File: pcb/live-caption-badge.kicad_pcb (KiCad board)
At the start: 4 copper layers, 170 x 100 mm, 102 parts, among them J1 Conn_01x09, J2 Conn_01x06, J3 Conn_01x09, J4 AudioJack4, J5 USB_C_Receptacle_USB2.0_16P, SW1 SW_DPDT_x2, SW2 RST, SW3 BTN, SW4 BTN, SW5 BTN, SW6 RST, U1 ESP32-S3-WROOM-1, U2 HE9073A33M5R, U3 HE9073A33M5R, U4 ES7210, U5 ES8311, U6 IS31AP2005

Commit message: pcb: Yippee
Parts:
- added R15: 1M, Resistor_SMD:R_0603_1608Metric, F.Cu at (74.0, 75.0)
- added R16: 2M, Resistor_SMD:R_0603_1608Metric, F.Cu at (74.0, 72.0)
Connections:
- U1 pad 15: unconnected-(U1-IO3-Pad15) -> /BATT_ADC
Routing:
- net /BATT_ADC: track 0.00 -> 26.7 mm
- net +BATT: track 50.2 -> 71.6 mm
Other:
- board text added: "M3"
- board text added: "yeah it wasn't soldered very well"

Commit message: pcb: Slap a KiCad logo on it
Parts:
- added REF**: KiCad-Logo2_8mm_Copper, Symbol:KiCad-Logo2_8mm_Copper, F.Cu at (180.0, 116.0)

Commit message: pcb: Edit a couple R/C values, generate BOM
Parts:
- R15: value 1M -> 150k
- R16: value 2M -> 300k
- R6: value 1k -> 5.1k
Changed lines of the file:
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@@
 			)
 		)
-		(property "Value" "1k"
+		(property "Value" "5.1k"
 			(at 0 1.43 0)
 			(layer "F.Fab")
@@
 		)
 		(fp_text user "${REFERENCE}"
-			(at 0 6.35 360)
+			(at 0 6.35 0)
 			(layer "F.Fab")
 			(effects
@@
 			)
 		)
-		(property "Value" "2M"
+		(property "Value" "300k"
 			(at 0 1.43 0)
 			(layer "F.Fab")
@@
 		(tags "resistor")
 		(property "Reference" "R15"
-			(at 0 1.5 360)
+			(at 0 1.5 0)
 			(layer "F.SilkS")
 			(effects
@@
 			)
 		)
-		(property "Value" "1M"
-			(at 0 1.43 360)
+		(property "Value" "150k"
+			(at 0 1.43 0)
 			(layer "F.Fab")
 			(effects
@@
 		)
 		(fp_text user "${REFERENCE}"
-			(at 0 0 360)
+			(at 0 0 0)
 			(layer "F.Fab")
 			(effects

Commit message: pcb: Rev 2 schematic
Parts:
- removed J1: Conn_01x09, live-caption-badge:Molex_CLIK-Mate_502386-0970_1x09-1MP_P1.25mm_Horizontal
- removed J3: Conn_01x09, Connector_PinHeader_2.54mm:PinHeader_1x09_P2.54mm_Vertical
- removed the REF** at (144.0, 102.5)
- removed the REF** at (144.0, 116.5)
- removed the REF** at (86.0, 102.5)
- removed the REF** at (144.0, 125.4)
- removed the REF** at (86.0, 125.4)
- removed the REF** at (86.0, 116.5)
- added C36: 1uF, Capacitor_SMD:C_0603_1608Metric, F.Cu at (225.2, 89.8)
- added C37: 10uF, Capacitor_SMD:C_0603_1608Metric, F.Cu at (225.2, 92.4)
- added C38: 1uF, Capacitor_SMD:C_0603_1608Metric, F.Cu at (225.2, 94.9)
- added C39: 1uF, Capacitor_SMD:C_0603_1608Metric, F.Cu at (225.2, 97.4)
- added C40: 1uF, Capacitor_SMD:C_0603_1608Metric, F.Cu at (225.2, 99.9)
- added C41: 10uF, Capacitor_SMD:C_0603_1608Metric, F.Cu at (229.2, 89.8)
- added C42: 10uF, Capacitor_SMD:C_0603_1608Metric, F.Cu at (229.2, 92.4)
- added C43: 10uF, Capacitor_SMD:C_0603_1608Metric, F.Cu at (229.2, 94.9)
- added C44: 10uF, Capacitor_SMD:C_0603_1608Metric, F.Cu at (229.2, 97.4)
- added C45: 1uF, Capacitor_SMD:C_0603_1608Metric, F.Cu at (229.2, 99.9)
- added C46: 10uF, Capacitor_SMD:C_0603_1608Metric, F.Cu at (233.2, 89.8)
- added C47: 4.7uF, Capacitor_SMD:C_0603_1608Metric, F.Cu at (235.0, 113.0)
- added C6: 47uF, Capacitor_SMD:C_0603_1608Metric, F.Cu at (239.2, 96.5)
- added D2: MBR0530, Diode_SMD:D_SOD-123, F.Cu at (244.0, 110.0)
- added D3: MBR0530, Diode_SMD:D_SOD-123, F.Cu at (244.0, 115.0)
- added D4: MBR0530, Diode_SMD:D_SOD-123, F.Cu at (244.0, 120.0)
- added Q1: Si1308EDL, Package_TO_SOT_SMD:SOT-323_SC-70, F.Cu at (235.0, 120.0)
- added R17: 0.47, Resistor_SMD:R_0603_1608Metric, F.Cu at (227.0, 121.0)
- added R7: 10k, Resistor_SMD:R_0603_1608Metric, F.Cu at (227.0, 118.0)
- added TP17: TestPoint, Connector_PinHeader_2.54mm:PinHeader_1x01_P2.54mm_Vertical, F.Cu at (133.0, 73.0)
- C1: footprint Capacitor_SMD:C_0603_1608Metric -> Capacitor_THT:CP_Radial_D8.0mm_P3.50mm
- moved C1 77.5 mm to (70.5, 111.0)
- moved J5 1.23 mm to (52.0, 32.1)
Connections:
- U1 pad 8: /SPI_CS -> /SPI_~{CS}
- U6 pad 5: /Audio/AUDIO_OUT -> Net-(C6-Pad1)
- U6 pad 8: GNDA -> unconnected-(U6-Pad8)
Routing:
- net /SPI_CS: track 70.7 -> 0.00 mm, vias 2 -> 0
- net /USB_D+: track 24.4 -> 0.00 mm
- net /USB_D-: track 24.2 -> 0.00 mm
- net Net-(J5-CC2): track 16.8 -> 0.00 mm
- net Net-(J5-CC1): track 14.5 -> 0.00 mm
- net GND: track 16.8 -> 4.86 mm
- net /Audio/AUDIO_OUT: track 56.3 -> 47.3 mm
- net +3V3: track 39.6 -> 32.4 mm
- net /EPD_PWR: track 83.3 -> 76.0 mm
- net /EPD_~{BUSY}: track 51.3 -> 44.6 mm
- net /SPI_MOSI: track 42.6 -> 36.4 mm
- net /SPI_SCK: track 44.0 -> 38.3 mm
- net /EPD_DC: track 60.9 -> 55.2 mm
- net GNDA: track 17.6 -> 19.3 mm
- net VBUS: track 54.1 -> 53.3 mm
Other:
- outline, holes or cut-outs redrawn
- board text removed: "BUSY"
- board text removed: "CS"
- board text removed: "DC"
- board text removed: "MOSI"
- board text removed: "PWR"
- board text removed: "RST"
- board text removed: "SCK"

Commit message: pcb: rev 2?
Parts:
- added J1: Conn_01x24, live-caption-badge:FPC05024-13200_1x24-1MP_P0.50_Horizontal, F.Cu at (115.0, 117.0)
- added L1: 68uH, live-caption-badge:L_Bourns-SDEE0406A, F.Cu at (123.5, 100.0)
- added Q2: SS8050, Package_TO_SOT_SMD:SOT-23, F.Cu at (110.0, 47.0)
- added Q3: SS8050, Package_TO_SOT_SMD:SOT-23, F.Cu at (110.0, 53.0)
- added R18: 10k, Resistor_SMD:R_0603_1608Metric, F.Cu at (115.0, 48.0)
- added R19: 10k, Resistor_SMD:R_0603_1608Metric, F.Cu at (115.0, 54.0)
- SW6: value RST -> FLASH
- moved C46 127.7 mm to (106.0, 101.0), turned to 180 degrees
- moved D4 124.5 mm to (120.0, 109.0), turned to 90 degrees
- moved C36 120.9 mm to (106.0, 110.0), turned to 180 degrees
- moved D3 120.1 mm to (124.0, 109.0), turned to -90 degrees
- moved C37 120.1 mm to (106.0, 107.0), turned to 180 degrees
- moved C38 119.5 mm to (106.0, 104.0), turned to 180 degrees
- moved D2 116.0 mm to (128.0, 109.0), turned to 90 degrees
- moved Q1 104.1 mm to (133.0, 99.0), turned to 90 degrees
- moved C47 102.0 mm to (133.0, 110.0), turned to 0 degrees
- moved C42 102.0 mm to (130.5, 118.0)
- moved C44 100.3 mm to (130.5, 115.0)
- moved C41 98.7 mm to (135.5, 121.0)
- moved C39 98.4 mm to (130.5, 124.0)
- moved C40 97.0 mm to (130.5, 121.0)
- moved C43 96.5 mm to (135.5, 118.0)
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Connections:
- C4 pad 1: /ESP_EN -> /ESP_~{EN}
- J2 pad 4: /ESP_IO0 -> /UART_RTS
- J2 pad 5: /ESP_EN -> /UART_DTR
- R1 pad 2: /ESP_EN -> /ESP_~{EN}
- SW2 pad 2: /ESP_EN -> /ESP_~{EN}
- U1 pad 19: /EPD_DC -> /EPD_~{BUSY}
- U1 pad 21: /SPI_SCK -> /EPD_DC
- U1 pad 22: /SPI_MOSI -> /SPI_~{CS}
- U1 pad 23: unconnected-(U1-IO21-Pad23) -> /SPI_SCK
- U1 pad 24: /EPD_~{BUSY} -> /SPI_MOSI
- U1 pad 3: /ESP_EN -> /ESP_~{EN}
- U1 pad 7: /EPD_PWR -> unconnected-(U1-IO7-Pad7)
- U1 pad 8: /SPI_~{CS} -> unconnected-(U1-IO15-Pad8)
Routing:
- net /ESP_~{EN}: track 0.00 -> 87.4 mm, vias 0 -> 2
- net /ESP_EN: track 79.2 -> 0.00 mm, vias 3 -> 0
- net /SPI_~{CS}: track 0.00 -> 76.8 mm
- net /EPD_PWR: track 76.0 -> 0.00 mm, vias 2 -> 0
- net /ESP_IO0: track 80.6 -> 38.7 mm, vias 3 -> 0
- net /SPI_MOSI: track 36.4 -> 77.2 mm, vias 1 -> 0
- net /SPI_SCK: track 38.3 -> 76.4 mm
- net /E-Paper/GDR: track 0.00 -> 36.3 mm, vias 0 -> 2
- net /E-Paper/RESE: track 0.00 -> 33.2 mm, vias 0 -> 2
- net /EPD_~{BUSY}: track 44.6 -> 77.7 mm, vias 1 -> 0
- net Net-(D4-A): track 0.00 -> 32.8 mm
- net /USB_D+: track 0.00 -> 26.4 mm
- net /USB_D-: track 0.00 -> 25.0 mm, vias 0 -> 2
- net /UART_RTS: track 0.00 -> 22.6 mm, vias 0 -> 1
- net /EPD_DC: track 55.2 -> 77.1 mm, vias 2 -> 0
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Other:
- outline, holes or cut-outs redrawn
- board text added: ":3"
- board text added: "BTN1"
- board text added: "BTN2"
- board text added: "BTN3"
- board text added: "DTR"
- board text added: "LIVE CAPTION BADGE REV 2 EECS 473 FA 2024"
- board text added: "RTS"
- board text added: "do not detonate"
- board text removed: "EN"
- board text removed: "IO0"
- board text removed: "LIVE CAPTION BADGE REV 1 EECS 473 FA 2024"

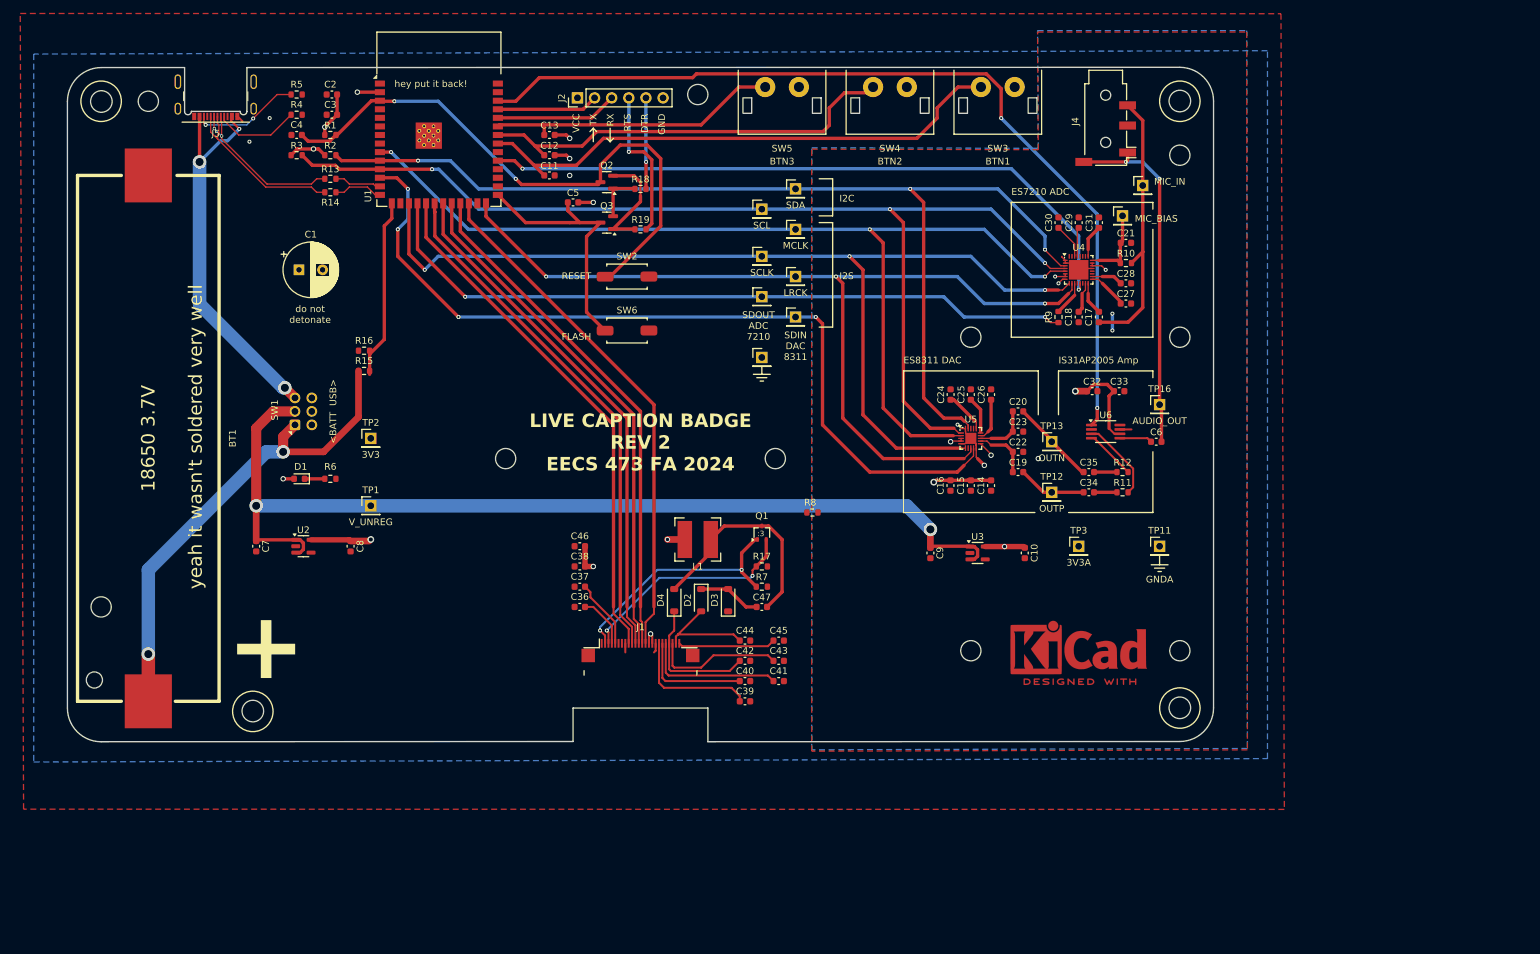
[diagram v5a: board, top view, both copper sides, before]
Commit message: pcb: Flip FPC, 170x105mm
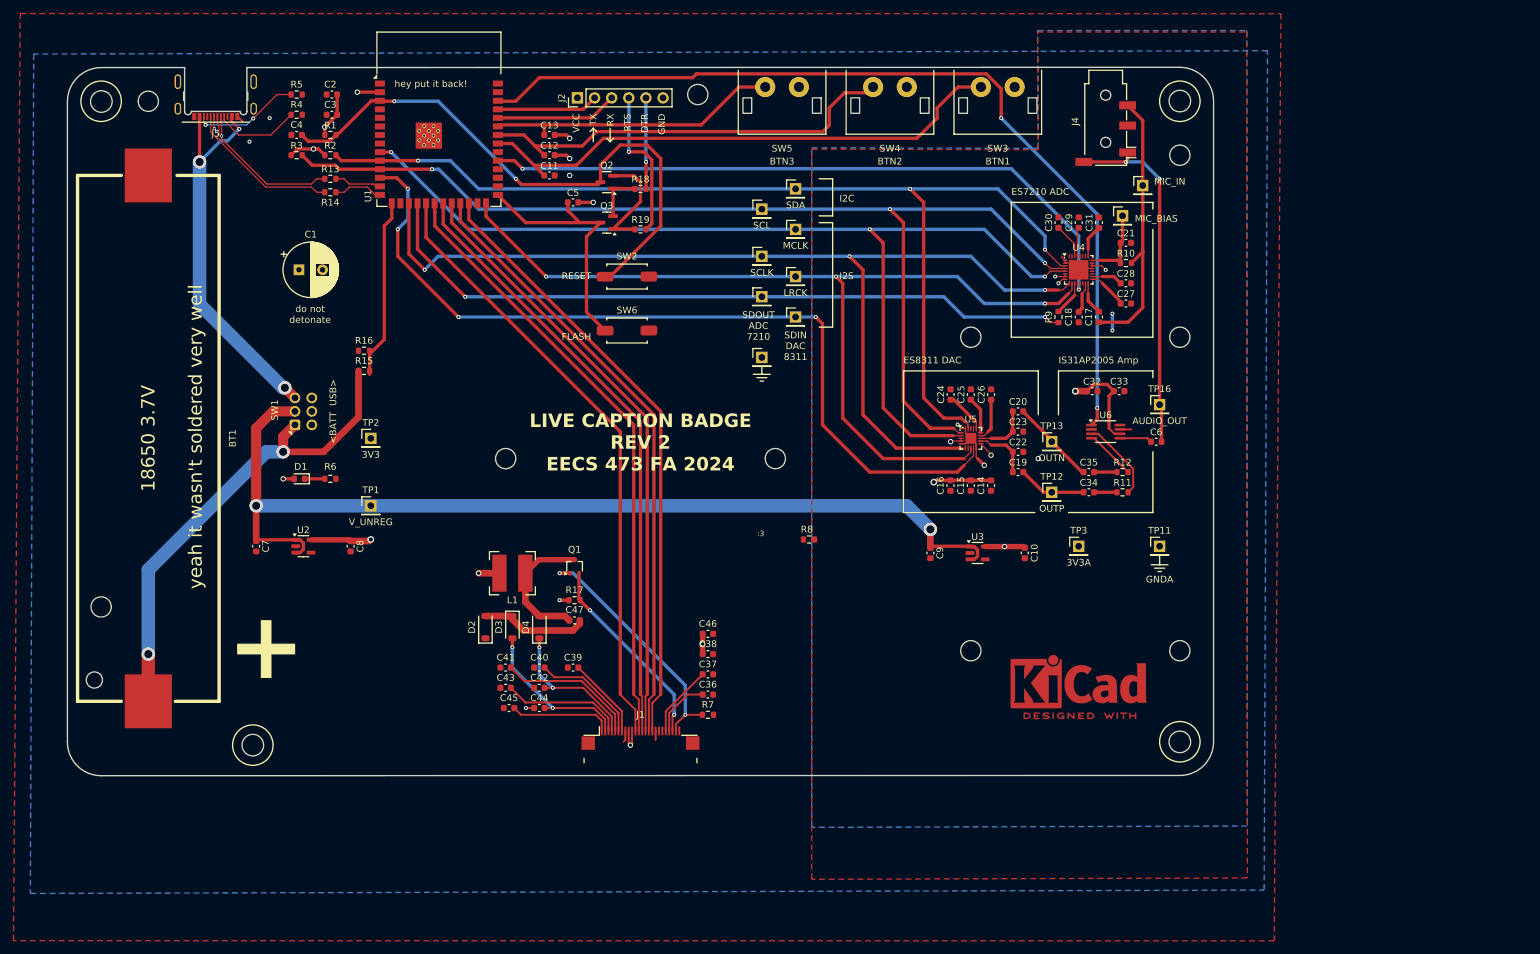
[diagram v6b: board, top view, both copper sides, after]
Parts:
- moved C45 41.2 mm to (95.5, 125.0), turned to 180 degrees
- moved C43 40.7 mm to (95.0, 122.0), turned to 180 degrees
- moved C41 40.5 mm to (95.0, 119.0), turned to 180 degrees
- moved D2 36.2 mm to (92.0, 113.0)
- moved C44 32.1 mm to (100.0, 125.0), turned to 180 degrees
- moved C42 30.8 mm to (100.0, 122.0), turned to 180 degrees
- moved C40 30.6 mm to (100.0, 119.0), turned to 180 degrees
- moved D3 28.3 mm to (96.0, 113.0)
- moved Q1 28.2 mm to (105.2, 104.0)
- moved R17 28.2 mm to (105.2, 109.0), turned to 180 degrees
- moved L1 28.0 mm to (96.0, 105.0)
- moved C47 27.8 mm to (105.2, 112.0), turned to 180 degrees
- moved C39 26.0 mm to (105.0, 119.0), turned to 180 degrees
- moved C36 23.0 mm to (125.0, 123.0), turned to 0 degrees
- moved C37 23.0 mm to (125.0, 120.0), turned to 0 degrees
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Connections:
- C36 pad 1: Net-(J1-Pin_4) -> Net-(J1-Pin_21)
- J1 pad 1: unconnected-(J1-Pin_1-Pad1) -> /E-Paper/VCOM
- J1 pad 10: /EPD_~{RST} -> +3V3
- J1 pad 11: /EPD_DC -> /SPI_MOSI
- J1 pad 12: /SPI_~{CS} -> /SPI_SCK
- J1 pad 13: /SPI_SCK -> /SPI_~{CS}
- J1 pad 14: /SPI_MOSI -> /EPD_DC
- J1 pad 15: +3V3 -> /EPD_~{RST}
- J1 pad 16: +3V3 -> /EPD_~{BUSY}
- J1 pad 18: /E-Paper/VDD -> unconnected-(J1-Pin_18-Pad18)
- J1 pad 19: /E-Paper/VOTP -> unconnected-(J1-Pin_19-Pad19)
- J1 pad 2: /E-Paper/GDR -> /E-Paper/PREVGL
- J1 pad 20: /E-Paper/VSH -> /E-Paper/VSHR
- J1 pad 21: /E-Paper/PREVGH -> Net-(J1-Pin_21)
- J1 pad 22: /E-Paper/VSL -> /E-Paper/RESE
- J1 pad 23: /E-Paper/PREVGL -> /E-Paper/GDR
- J1 pad 24: /E-Paper/VCOM -> unconnected-(J1-Pin_24-Pad24)
- J1 pad 3: /E-Paper/RESE -> /E-Paper/VSL
- J1 pad 4: Net-(J1-Pin_4) -> /E-Paper/PREVGH
- J1 pad 5: /E-Paper/VSHR -> /E-Paper/VSH
- J1 pad 6: unconnected-(J1-Pin_6-Pad6) -> /E-Paper/VOTP
- J1 pad 7: unconnected-(J1-Pin_7-Pad7) -> /E-Paper/VDD
- J1 pad 9: /EPD_~{BUSY} -> +3V3
- U1 pad 19: /EPD_~{BUSY} -> /SPI_MOSI
- U1 pad 20: /EPD_~{RST} -> /SPI_SCK
- U1 pad 21: /EPD_DC -> /SPI_~{CS}
- U1 pad 22: /SPI_~{CS} -> /EPD_DC
- U1 pad 23: /SPI_SCK -> /EPD_~{RST}
- U1 pad 24: /SPI_MOSI -> /EPD_~{BUSY}
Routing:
- net /SPI_SCK: track 76.4 -> 90.8 mm
- net /SPI_MOSI: track 77.2 -> 91.1 mm
- net /SPI_~{CS}: track 76.8 -> 90.5 mm
- net /EPD_DC: track 77.1 -> 90.4 mm
- net /EPD_~{RST}: track 77.4 -> 90.5 mm
- net /EPD_~{BUSY}: track 77.7 -> 90.6 mm
- net Net-(D4-A): track 32.8 -> 20.1 mm
- net Net-(J1-Pin_21): track 0.00 -> 8.76 mm
- net /E-Paper/PREVGL: track 15.8 -> 24.2 mm, vias 0 -> 2
- net Net-(J1-Pin_4): track 7.76 -> 0.00 mm
- net /E-Paper/VDD: track 19.4 -> 12.1 mm
- net Net-(D2-A): track 9.32 -> 16.3 mm
- net /E-Paper/RESE: track 33.2 -> 29.4 mm
- net GND: track 11.2 -> 14.0 mm, vias 6 -> 8
- net /E-Paper/PREVGH: track 20.1 -> 22.1 mm, vias 0 -> 2
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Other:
- board size 170 x 100 mm -> 170 x 105.1 mm
